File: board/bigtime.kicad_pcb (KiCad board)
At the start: 2 copper layers, 90 x 142 mm, 122 parts, among them IC1 NPIC6C596A, IC2 TPS62152, IC3 25AA02E48, IC4 STM32F407VET6, IC5 KSZ8081RNx, IC6 MAX5969x, IC7 MAX17503, IC8 LDL212DR, J1 RJHSE-538B, J2 MICROUSB, P1 CONN_IN, P2 CONN_OUT, P3 +12V, P4 SWD_TC, P5 SWD, T1 749010012A, U1 SA40-19, X1 M3_HOLE, X2 M3_HOLE, X3 M3_HOLE, X4 M3_HOLE, Y1 26M, Y2 25MHz, Y3 32.768k

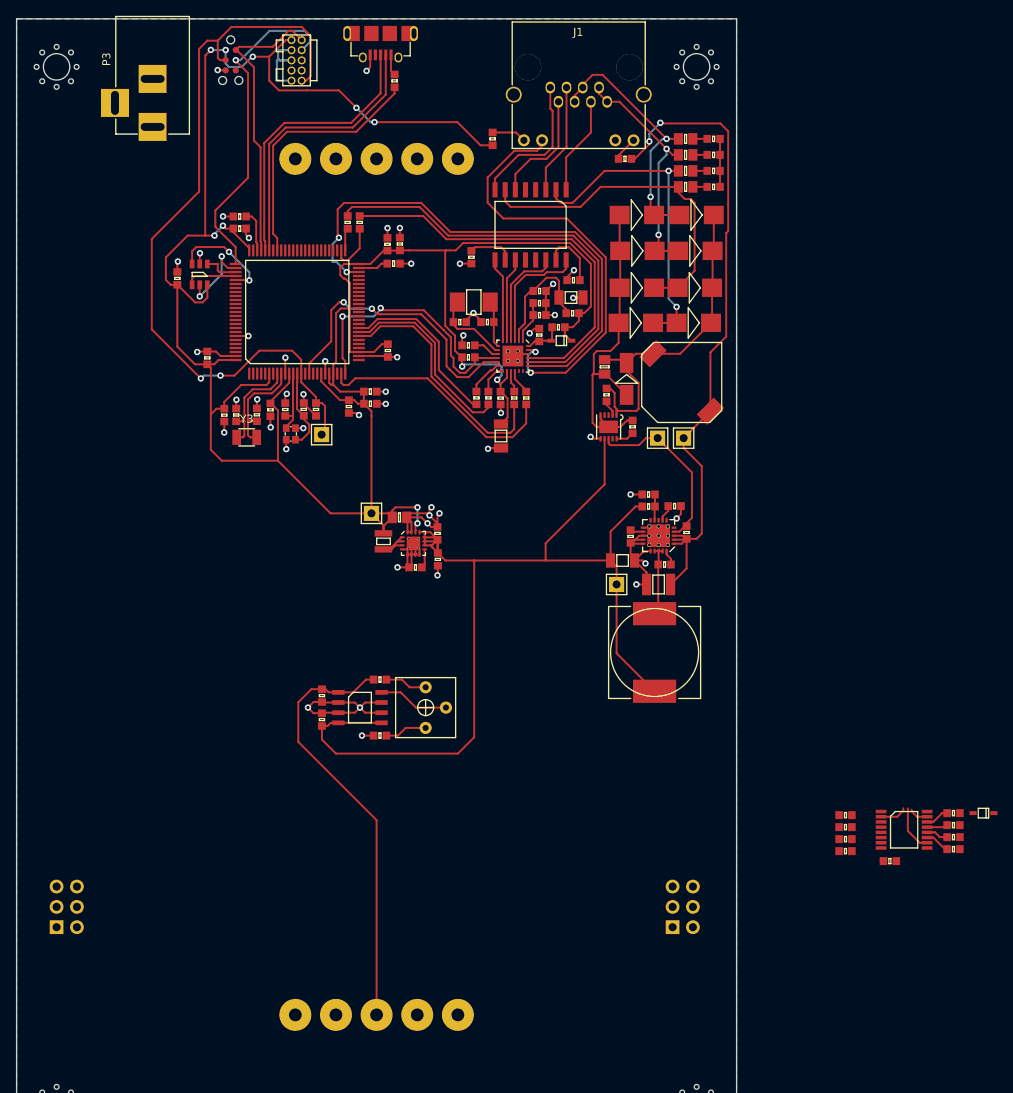
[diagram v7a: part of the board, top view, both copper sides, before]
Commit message: Finished first (pretty awful) route
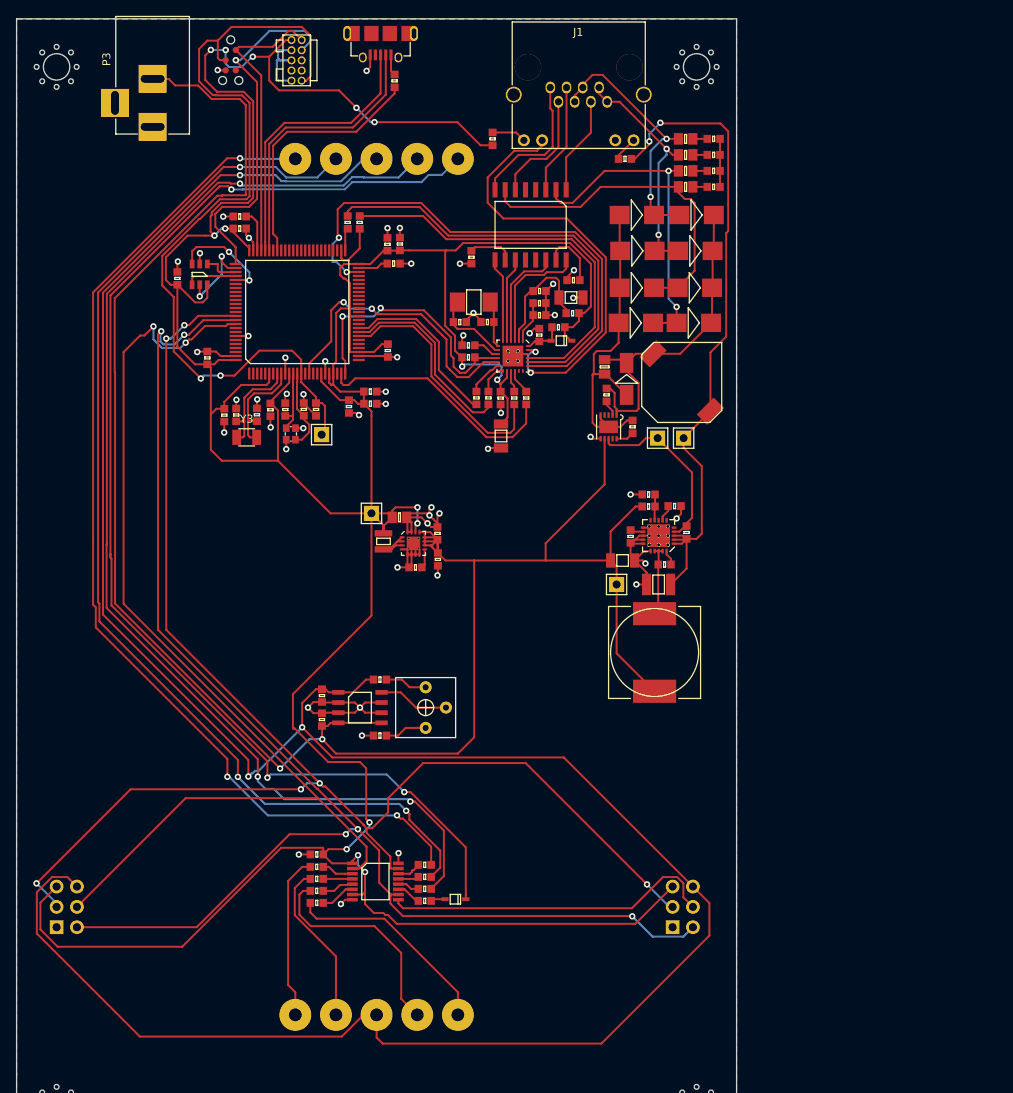
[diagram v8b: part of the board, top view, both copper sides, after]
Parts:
- moved C1 71.6 mm to (162.5, 123.4)
- moved D1 66.9 mm to (179.8, 129.0)
- moved IC1 66.4 mm to (169.8, 126.8)
- moved R1 66.4 mm to (162.5, 125.0)
- moved R10 66.4 mm to (176.0, 124.8)
- moved R4 66.4 mm to (162.5, 126.5)
- moved R5 66.4 mm to (162.5, 128.0)
- moved R6 66.4 mm to (162.5, 129.5)
- moved R7 66.4 mm to (176.0, 129.2)
- moved R8 66.4 mm to (176.0, 127.8)
- moved R9 66.4 mm to (176.0, 126.2)
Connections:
- D1 pad 2: Net-(D1-Pad2) -> /LED_DP
- R1 pad 1: Net-(R1-Pad1) -> /LED_G
- R10 pad 1: Net-(D1-Pad2) -> /LED_E
- R4 pad 1: Net-(R4-Pad1) -> /LED_F
- R5 pad 1: Net-(R5-Pad1) -> /LED_A
- R6 pad 1: Net-(R6-Pad1) -> /LED_B
- R7 pad 1: Net-(R7-Pad1) -> /LED_DP
- R8 pad 1: Net-(R8-Pad1) -> /LED_C
- R9 pad 1: Net-(R9-Pad1) -> /LED_D
- U1 pad 1: Net-(R7-Pad1) -> /LED_E
- U1 pad 10: Net-(R9-Pad1) -> /LED_G
- U1 pad 2: Net-(R6-Pad1) -> /LED_D
- U1 pad 4: Net-(R5-Pad1) -> /LED_C
- U1 pad 6: Net-(R4-Pad1) -> /LED_B
- U1 pad 7: Net-(R1-Pad1) -> /LED_A
- U1 pad 9: Net-(R8-Pad1) -> /LED_F
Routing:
- net /V_LED_BUS: track 54.0 -> 307.3 mm, vias 0 -> 3
- net /SHCP: track 2.43 -> 183.5 mm, vias 0 -> 6
- net /STCP: track 5.83 -> 177.1 mm, vias 0 -> 5
- net +3V3: track 318.3 -> 486.9 mm, vias 11 -> 15
- net Net-(D1-Pad1): track 0.00 -> 154.6 mm, vias 0 -> 3
- net /LED_C: track 0.00 -> 148.6 mm, vias 0 -> 3
- net /LED_D: track 0.00 -> 138.9 mm, vias 0 -> 3
- net /LED_E: track 0.00 -> 131.1 mm, vias 0 -> 3
- net /DS_IN: track 3.40 -> 132.8 mm, vias 0 -> 2
- net +12V: track 135.2 -> 255.4 mm, vias 0 -> 2
- net /DS_OUT: track 0.00 -> 41.7 mm
- net /LED_A: track 0.00 -> 27.4 mm
- net /LED_B: track 0.00 -> 26.6 mm
- net /LED_G: track 0.00 -> 20.6 mm
- net /LED_F: track 0.00 -> 20.4 mm
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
